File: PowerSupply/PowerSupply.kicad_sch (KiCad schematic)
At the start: 25 parts, among them J1 AC+, J2 AC-, J3 POWER, U1 LM317_SOT-223, U2 LM337_SOT223

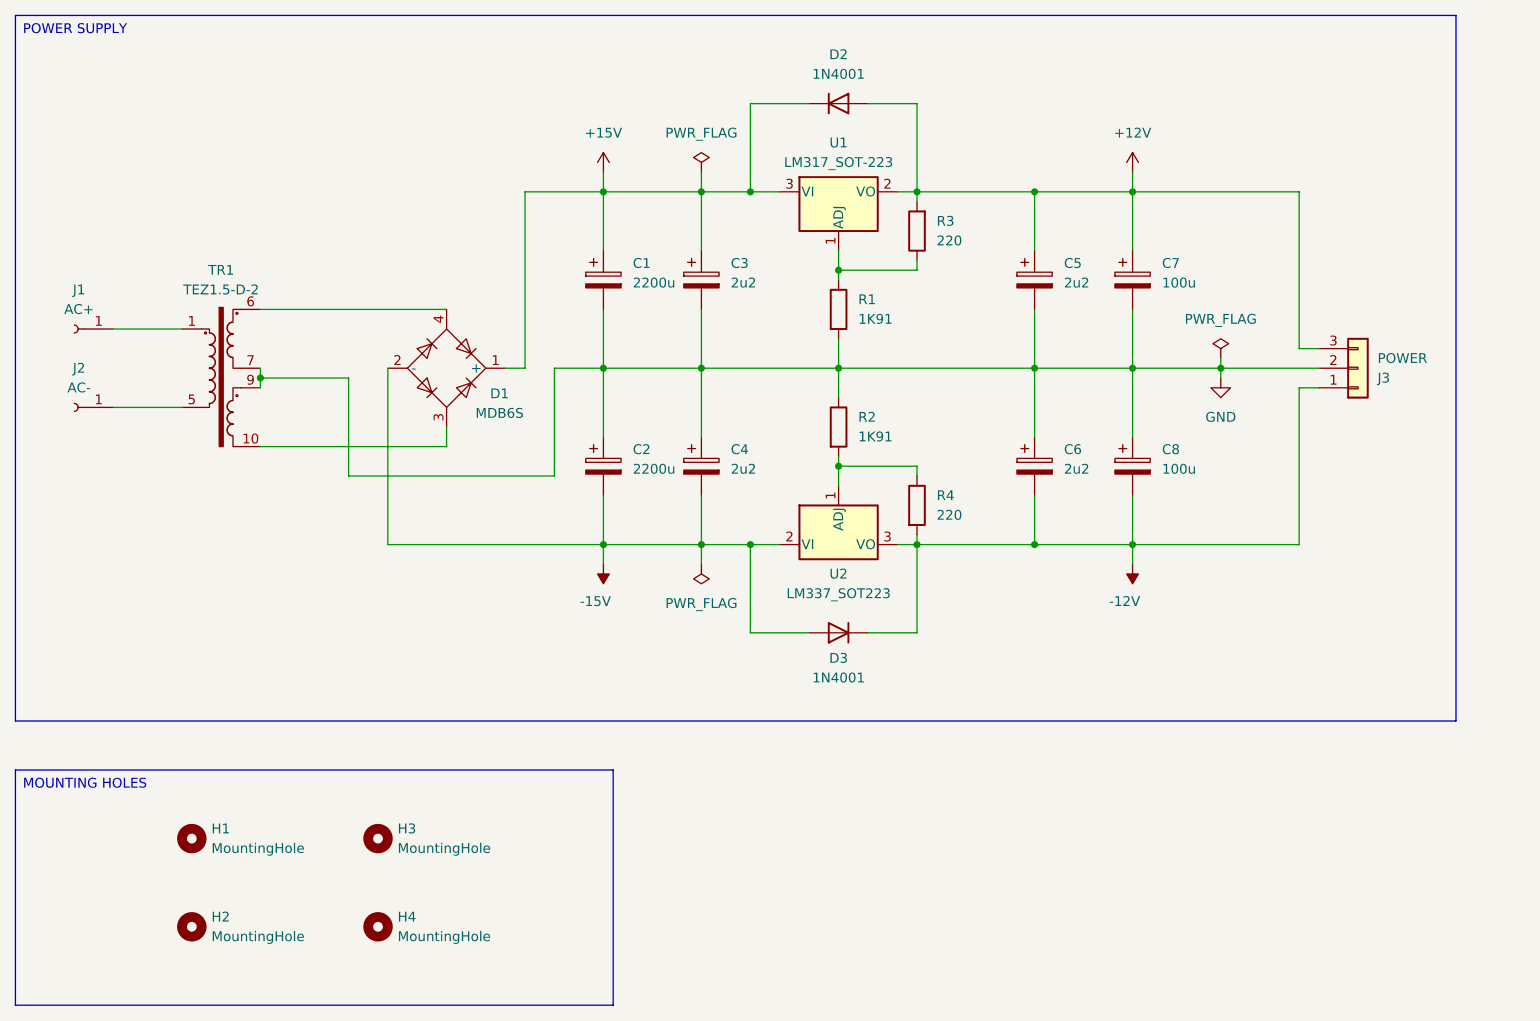
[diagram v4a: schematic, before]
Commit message: Power Supply Design
Updated the power supply schematic.
Updated the power supply board design.
Set the power supply project version to 1.1.
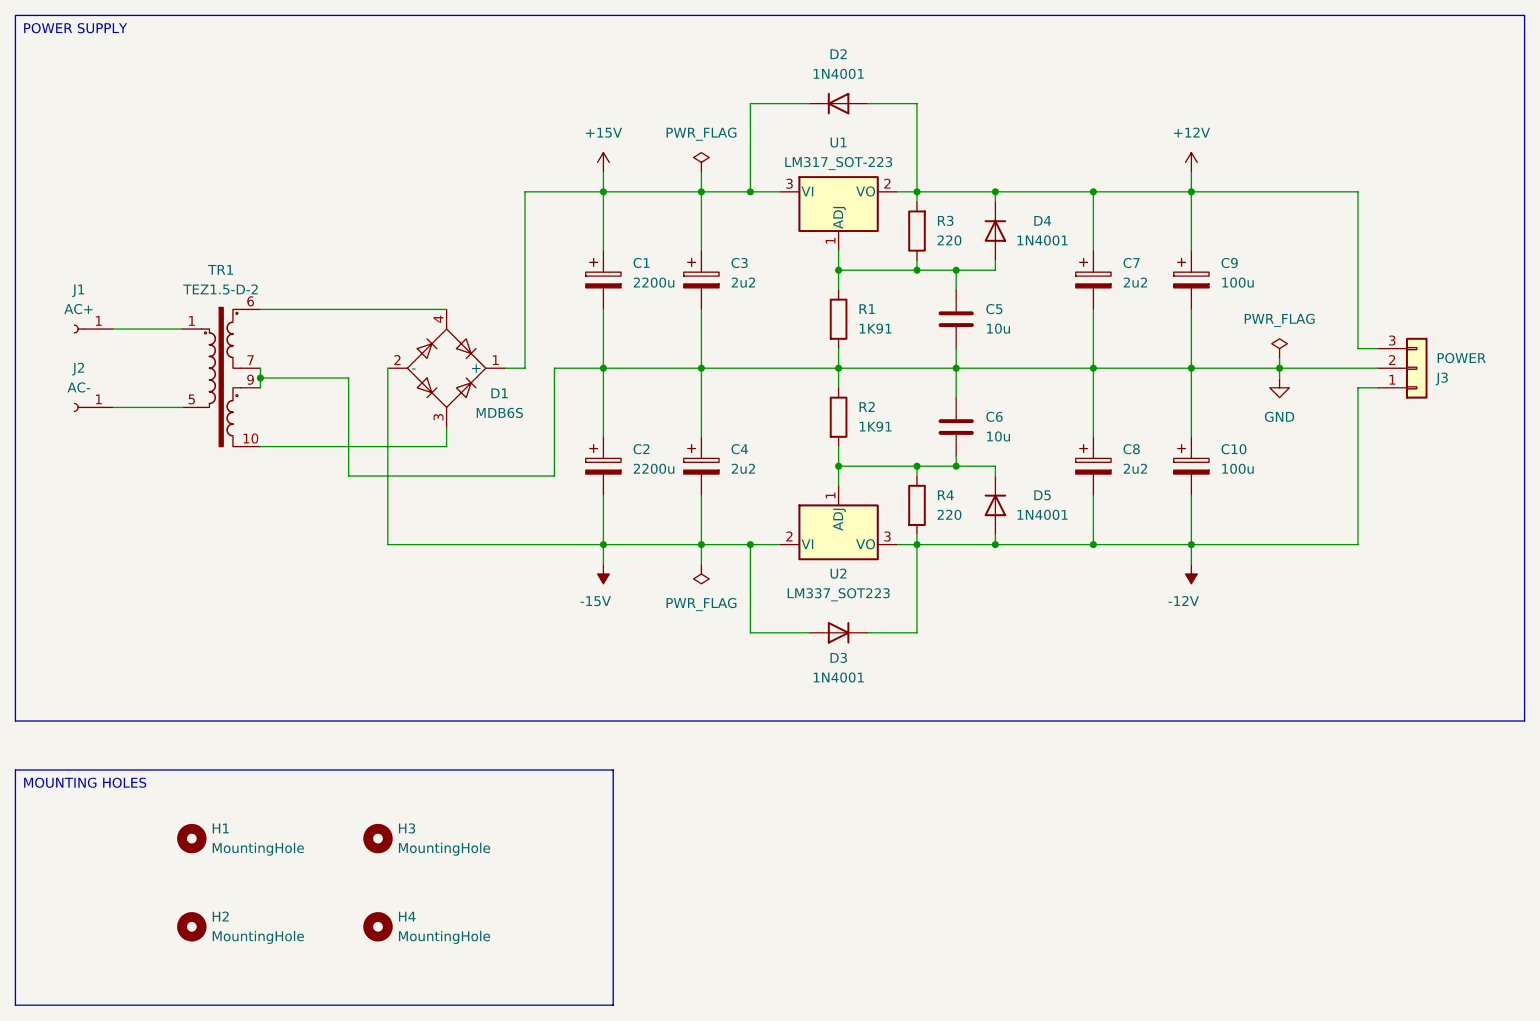
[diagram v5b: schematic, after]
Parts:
- added C5, C6: 10u, Capacitor_SMD:C_0805_2012Metric_Pad1.18x1.45mm_HandSolder, symbol Device:C
- added D4, D5: 1N4001, Diode_SMD:D_SOD-323, symbol Diode:1N4001
- renumbered C8 to C10, C5 to C7, C6 to C8, C7 to C9
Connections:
- net +12V: now also D4.1 (K)
- net -12V: now also D5.2 (A)
- net GND: now also C5.2, C6.1
- net at R1.1, R3.1, U1.1 (ADJ): now also C5.1, D4.2 (A)
- net at R2.2, R4.1, U2.1 (ADJ): now also C6.2, D5.1 (K)
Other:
- moved on the sheet: C10, C7, C8, C9, J3, R1, R2

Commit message: Company name
Updated the company name for all project files.
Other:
- company: Chapuzas S.L. -> DavidMolTor
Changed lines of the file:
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@@
 		(date "2025-08-08")
 		(rev "1.1")
-		(company "Chapuzas S.L.")
+		(company "DavidMolTor")
 	)
 	(text_box "POWER SUPPLY"
